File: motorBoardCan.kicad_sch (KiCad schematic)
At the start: 21 parts, among them J1 Conn_01x04_Pin, J2 Conn_01x04_Pin, J3 Conn_02x04_Top_Bottom, J6 Conn_02x04_Top_Bottom, U1 NUCLEO-G431KB, U4 SN65HVD230, U5 LD1117S33TR_SOT223

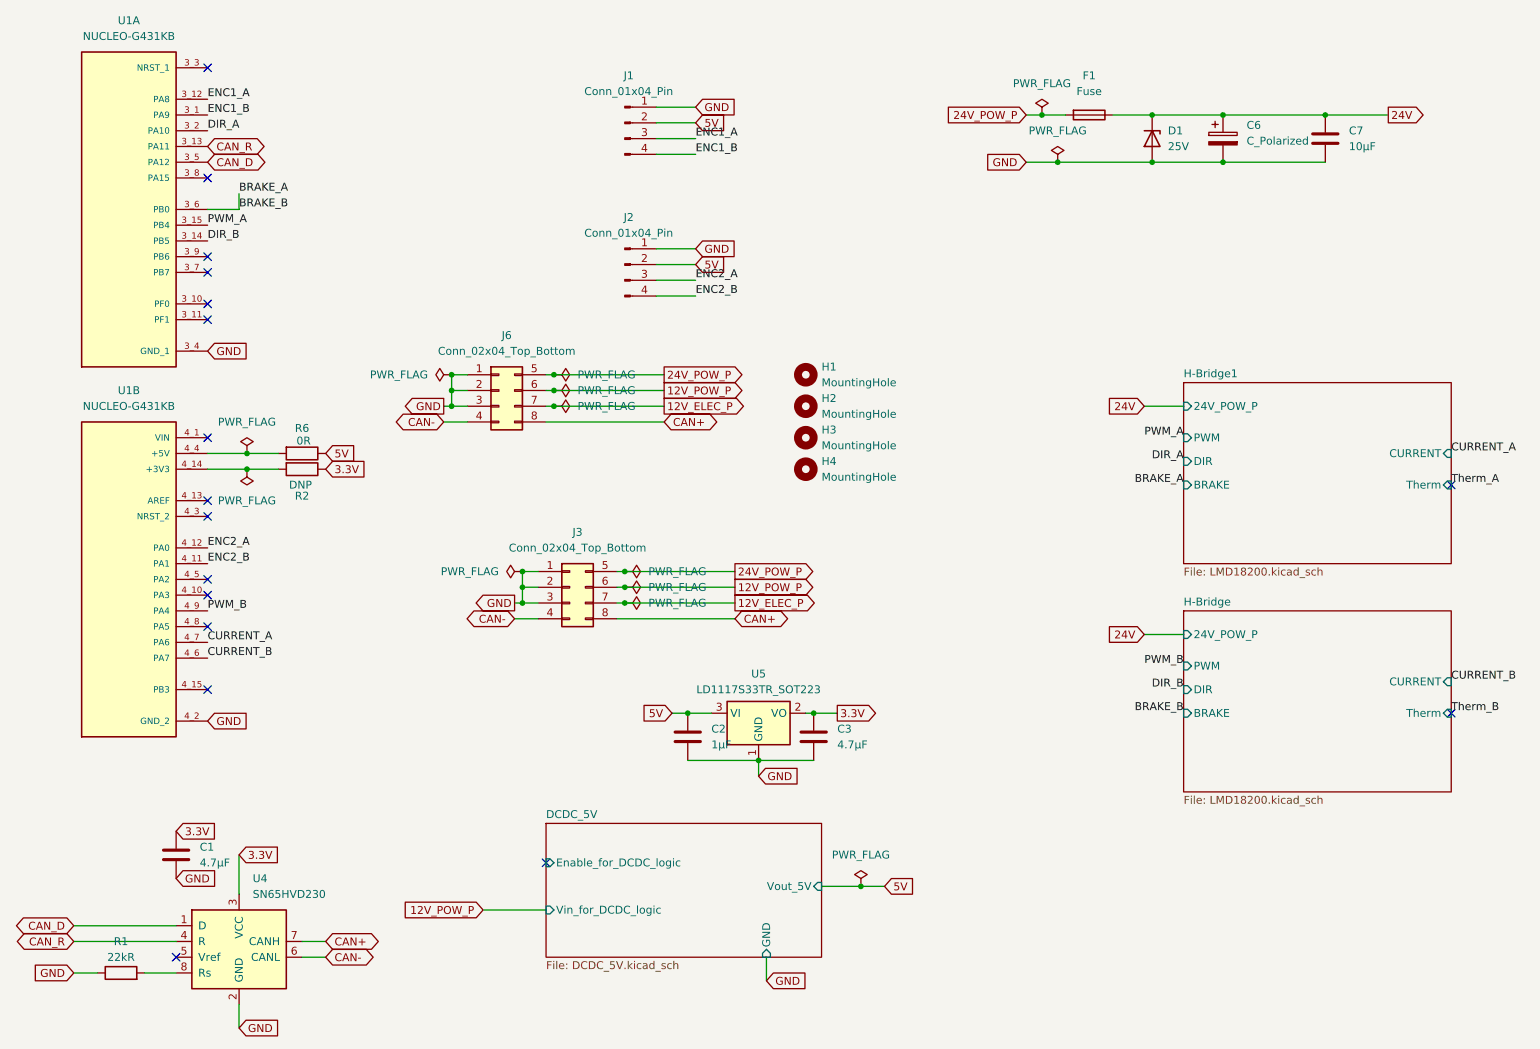
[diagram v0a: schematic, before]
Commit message: fix warning, separate brake commands, add JLCJLCJLC, enlarge capacitors, tune routing
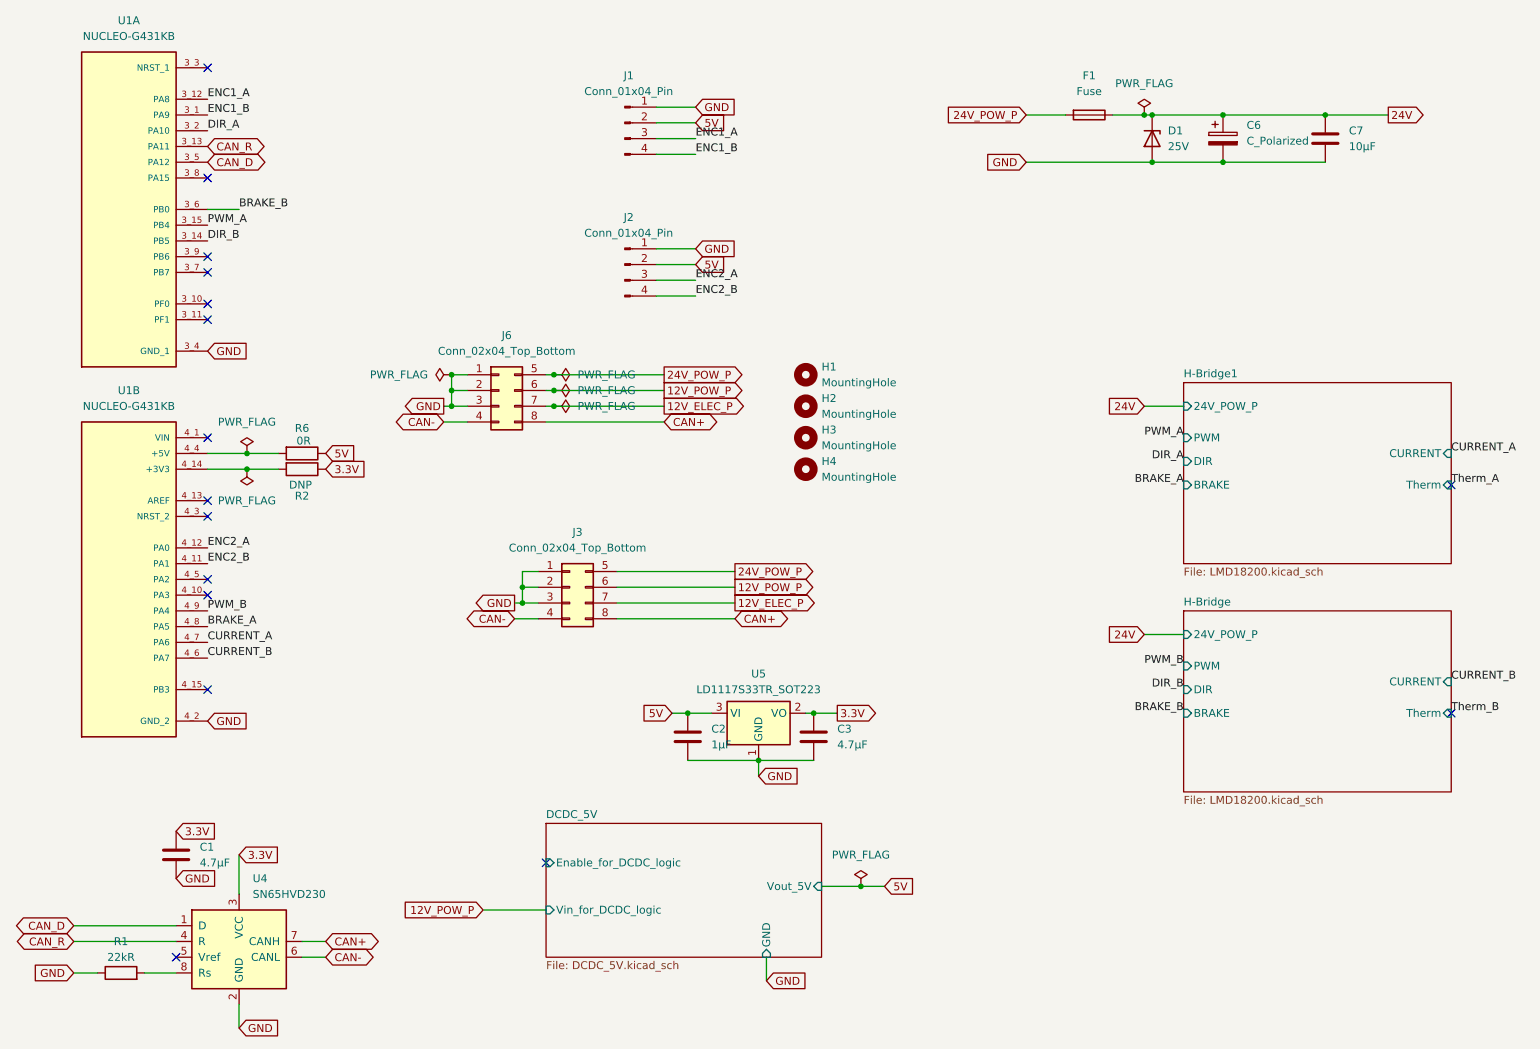
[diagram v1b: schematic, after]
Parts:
- C1, C2, C3: footprint Capacitor_SMD:C_0603_1608Metric -> Capacitor_SMD:C_1206_3216Metric
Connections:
- net BRAKE_A: now also U1.4_8 (PA5); no longer U1.3_6 (PB0)
- new net BRAKE_B: U1.3_6 (PB0)
- no-connect marks 17 -> 16

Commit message: Add BOM
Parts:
- C1, C3: LCSC# (none) -> C29823
- C2: LCSC# (none) -> C91151
- C6: LCSC# (none) -> C398835
- C7: value 10µF -> 10uF; LCSC# (none) -> C1713
- D1: footprint Diode_SMD:D_1206_3216Metric -> Capacitor_SMD:C_0805_2012Metric; LCSC# (none) -> C118721
- F1: LCSC# (none) -> C27515
- J1, J2: LCSC# (none) -> C2691448
- J3, J6: LCSC# (none) -> C277661
- R1: LCSC# (none) -> C2907128
- R6: LCSC# (none) -> C2930117
- U4: LCSC# (none) -> C12084
- U5: LCSC# (none) -> C20538890
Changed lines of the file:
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@@
 	(label "BRAKE_A"
 		(at 215.9 101.6 180)
-		(fields_autoplaced yes)
 		(effects
 			(font
@@
 	(label "CURRENT_B"
 		(at 259.08 133.35 0)
-		(fields_autoplaced yes)
 		(effects
 			(font
@@
 	(label "DIR_A"
 		(at 215.9 97.79 180)
-		(fields_autoplaced yes)
 		(effects
 			(font
@@
 	(label "Therm_B"
 		(at 259.08 138.43 0)
-		(fields_autoplaced yes)
 		(effects
 			(font
@@
 	(label "BRAKE_B"
 		(at 63.5 57.15 0)
-		(fields_autoplaced yes)
 		(effects
 			(font
@@
 	(label "PWM_A"
 		(at 215.9 93.98 180)
-		(fields_autoplaced yes)
 		(effects
 			(font
@@
 	(label "BRAKE_A"
 		(at 58.42 124.46 0)
-		(fields_autoplaced yes)
 		(effects
 			(font
@@
 	(label "ENC2_A"
 		(at 58.42 111.76 0)
-		(fields_autoplaced yes)
 		(effects
 			(font
@@
 	(label "ENC1_A"
 		(at 137.16 45.72 0)
-		(fields_autoplaced yes)
 		(effects
 			(font
@@
 	(label "ENC1_B"
 		(at 58.42 41.91 0)
-		(fields_autoplaced yes)
 		(effects
 			(font
@@
 	(label "ENC1_A"
 		(at 58.42 39.37 0)
-		(fields_autoplaced yes)
 		(effects
 			(font
@@
 	(label "ENC2_B"
 		(at 137.16 71.12 0)
-		(fields_autoplaced yes)
 		(effects
 			(font
@@
 	(label "PWM_B"
 		(at 215.9 130.81 180)
-		(fields_autoplaced yes)
 		(effects
 			(font
@@
 	(label "PWM_B"
 		(at 58.42 121.92 0)
-		(fields_autoplaced yes)
 		(effects
 			(font
@@
 	(label "ENC2_B"
 		(at 58.42 114.3 0)
-		(fields_autoplaced yes)
 		(effects
 			(font
@@
 	(label "BRAKE_B"
 		(at 215.9 138.43 180)
-		(fields_autoplaced yes)
 		(effects
 			(font
@@
 	(label "PWM_A"
 		(at 58.42 59.69 0)
-		(fields_autoplaced yes)
 		(effects
 			(font
@@
 	(label "DIR_B"
 		(at 215.9 134.62 180)
-		(fields_autoplaced yes)
 		(effects
 			(font
@@
 	(label "DIR_B"
 		(at 58.42 62.23 0)
-		(fields_autoplaced yes)
 		(effects
 			(font
@@
 	(label "CURRENT_A"
 		(at 259.08 96.52 0)
-		(fields_autoplaced yes)
 		(effects
 			(font
@@
 	(label "CURRENT_B"
 		(at 58.42 129.54 0)
-		(fields_autoplaced yes)
 		(effects
 			(font
@@
 	(label "DIR_A"
 		(at 58.42 44.45 0)
-		(fields_autoplaced yes)
 		(effects
 			(font
@@
 	(label "ENC1_B"
 		(at 137.16 48.26 0)
-		(fields_autoplaced yes)
 		(effects
 			(font
@@
 	(label "Therm_A"
 		(at 259.08 101.6 0)
-		(fields_autoplaced yes)
 		(effects
 			(font
@@
 	(label "CURRENT_A"
 		(at 58.42 127 0)
-		(fields_autoplaced yes)
 		(effects
 			(font
@@
 	(label "ENC2_A"
 		(at 137.16 68.58 0)
-		(fields_autoplaced yes)
 		(effects
 			(font
@@
 			)
 		)
+		(property "LCSC#" "C2907128"
+			(at 44.45 180.34 0)
+			(effects
+				(font
+					(size 1.27 1.27)
+				)
+				(hide yes)
+			)
+		)
 		(pin "1"
 		)
@@
 			)
 		)
+		(property "LCSC#" "C398835"
+			(at 222.25 45.72 0)
+			(effects
+				(font
+					(size 1.27 1.27)
+				)
+				(hide yes)
+			)
+		)
 		(pin "1"
 		)
@@
 			)
 		)
+		(property "LCSC#" "C277661"
+			(at 105.41 86.36 0)
+			(effects
+				(font
+					(size 1.27 1.27)
+				)
+				(hide yes)
+			)
+		)
 		(pin "1"
 		)
@@
 			)
 		)
-		(property "Footprint" "Diode_SMD:D_1206_3216Metric"
+		(property "Footprint" "Capacitor_SMD:C_0805_2012Metric"
 			(at 210.82 45.72 0)
 			(effects
@@
 			)
 		)
+		(property "LCSC#" "C118721"
+			(at 210.82 45.72 0)
+			(effects
+				(font
+					(size 1.27 1.27)
+				)
+				(hide yes)
+			)
+		)
 		(pin "1"
 		)
@@
 			)
 		)
+		(property "LCSC#" "C20538890"
+			(at 147.32 138.43 0)
+			(effects
+				(font
+					(size 1.27 1.27)
+				)
+				(hide yes)
+			)
+		)
 		(pin "1"
 		)
@@
 			)
 		)
+		(property "LCSC#" "C29823"
+			(at 53.34 161.29 0)
+			(effects
+				(font
+					(size 1.27 1.27)
+				)
+				(hide yes)
+			)
+		)
 		(pin "1"
 		)
@@
 			)
 		)
+		(property "LCSC#" "C27515"
+			(at 200.66 41.91 0)
+			(effects
+				(font
+					(size 1.27 1.27)
+				)
+				(hide yes)
+			)
+		)
 		(pin "1"
 		)
@@
 			)
 		)
+		(property "LCSC#" "C2691448"
+			(at 125.73 66.04 0)
+			(effects
+				(font
+					(size 1.27 1.27)
+				)
+				(hide yes)
+			)
+		)
 		(pin "2"
 		)
@@
 			)
 		)
+		(property "LCSC#" ""
+			(at 154.94 83.82 0)
+			(effects
+				(font
+					(size 1.27 1.27)
+				)
+				(hide yes)
+			)
+		)
 		(instances
 			(project ""
@@
 			)
 		)
+		(property "LCSC#" "C29823"
+			(at 156.21 142.24 0)
+			(effects
+				(font
+					(size 1.27 1.27)
+				)
+				(hide yes)
+			)
+		)
 		(pin "1"
 		)
@@
 			)
 		)
+		(property "LCSC#" "C2930117"
+			(at 73.66 96.52 0)
+			(effects
+				(font
+					(size 1.27 1.27)
+				)
+				(hide yes)
+			)
+		)
 		(pin "1"
 		)
@@
 			)
 		)
+		(property "LCSC#" ""
+			(at 45.72 116.84 0)
+			(effects
+				(font
+					(size 1.27 1.27)
+				)
+				(hide yes)
+			)
+		)
 		(pin "3_5"
 		)
@@
 			)
 		)
+		(property "LCSC#" ""
+			(at 154.94 88.9 0)
+			(effects
+				(font
+					(size 1.27 1.27)
+				)
+				(hide yes)
+			)
+		)
 		(instances
 			(project "motorBoardCan"
@@
 			)
 		)
+		(property "LCSC#" "C277661"
+			(at 116.84 118.11 0)
+			(effects
+				(font
+					(size 1.27 1.27)
+				)
+				(hide yes)
+			)
+		)
 		(pin "1"
 		)
@@
 			)
 		)
+		(property "LCSC#" "C12084"
+			(at 63.5 175.26 0)
+			(effects
+				(font
+					(size 1.27 1.27)
+				)
+				(hide yes)
+			)
+		)
 		(pin "2"
 		)
@@
 			)
 		)
+		(property "LCSC#" ""
+			(at 73.66 99.06 0)
+			(effects
+				(font
+					(size 1.27 1.27)
+				)
+				(hide yes)
+			)
+		)
 		(pin "1"
 		)
@@
 			)
 		)
-		(property "Value" "10µF"
+		(property "Value" "10uF"
 			(at 242.57 46.9899 0)
 			(effects
@@
 			)
 		)
+		(property "LCSC#" "C1713"
+			(at 238.76 45.72 0)
+			(effects
+				(font
+					(size 1.27 1.27)
+				)
+				(hide yes)
+			)
+		)
 		(pin "1"
 		)
@@
 			)
 		)
+		(property "LCSC#" "C91151"
+			(at 135.89 142.24 0)
+			(effects
+				(font
+					(size 1.27 1.27)
+				)
+				(hide yes)
+			)
+		)
 		(pin "1"
 		)
@@
 			)
 		)
+		(property "LCSC#" ""
+			(at 154.94 99.06 0)
+			(effects
+				(font
+					(size 1.27 1.27)
+				)
+				(hide yes)
+			)
+		)
 		(instances
 			(project "motorBoardCan"
@@
 			)
 		)
+		(property "LCSC#" ""
+			(at 45.72 57.15 0)
+			(effects
+				(font
+					(size 1.27 1.27)
+				)
+				(hide yes)
+			)
+		)
 		(pin "3_5"
 		)
@@
 			)
 		)
+		(property "LCSC#" ""
+			(at 154.94 93.98 0)
+			(effects
+				(font
+					(size 1.27 1.27)
+				)
+				(hide yes)
+			)
+		)
 		(instances
 			(project "motorBoardCan"
@@
 			(at 125.73 43.18 0)
 			(effects
+				(font
+					(size 1.27 1.27)
+				)
+				(hide yes)
+			)
+		)
+		(property "LCSC#" "C2691448"
+			(at 125.73 43.18 0)
+			(effects
